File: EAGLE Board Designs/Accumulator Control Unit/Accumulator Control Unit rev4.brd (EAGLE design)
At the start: 186.7 x 135.7 mm, 241 parts, among them J1 CONNECTOR-2_MF_T_V_, J100 CONNECTOR-8_S_S, J2 CONNECTOR-8_MF_T_V_, J3 CONNECTOR-14_MF_T_V_, J4 JUMPER__1X02, J5 CONNECTOR-12_MF_T_V_, J6 CONNECTOR-CAN_μF_S_RA_, Q1 TRANSISTOR_N_MOS__PMV15ENEA, Q100 TRANSISTOR_N_MOS__PMV15ENEA, Q101 TRANSISTOR_N_MOS__PMV15ENEA, Q2 TRANSISTOR_N_MOS__PMV15ENEA, T1 TRANSFORMER_HM2112ZNLT_AIRGAP, U1 RELAY_SOLIDSTATE_NO, U10 MAX7404, U100 ADG1423, U101 LM555, U11 OPAMP_1_CHANNEL_OPA991, U12 LOGICGATE_AND_DCK3, U13 OPAMP_1_CHANNEL_OPA991, U14 LOGICGATE_AND_DCK3, U15 OPAMP_1_CHANNEL_OPA991, U16 LOGICGATE_AND_DCK3, U17 OPAMP_1_CHANNEL_OPA991, U18 OPAMP_1_CHANNEL_OPA991, U19 MAX7404, U2 RELAY_SOLIDSTATE_NO, U20 OPAMP_1_CHANNEL_OPA991, U21 OPAMP_1_CHANNEL_OPA991, U22 OPAMP_1_CHANNEL_OPA991, U23 OPAMP_1_CHANNEL_OPA991, U24 OPAMP_1_CHANNEL_OPA991, U25 MAX7404, U26 VOLTAGE_REGULATOR_SOT223_3.3V, U27 TCAN1051HQV-Q1, U3 OPAMP_1_CHANNEL_OPA991, U4 MAX7404, U5 LTC6820, U6 LOGICGATE_BUFFER, U7 ADM8316WBX30, U8 RELAY_SOLIDSTATE_NO, U9 OPAMP_1_CHANNEL_OPA991

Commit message: uncursed library
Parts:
- added A3: VOLTAGE_REGULATOR_MODULE_OKI-78SR_12V, HyTechDevices:OKI-78SR
- added TP1_24V: TEST_POINT, HyTechDevices:5015
- J3: device HyTechDevices - Copy:MOLEX_MICROFIT_PTH_VERTICAL_14_DUAL -> HyTechDevices:MOLEX_MICROFIT_PTH_VERTICAL_14_DUAL
- TP_12V, TP_3.3V, TP_5V, TP_GND: device HyTechDevices - Copy:MICRO_MINIATURE -> HyTechDevices:5015
- U1, U2, U8: value RELAY_SOLIDSTATE_NO -> RELAY_SOLIDSTATE_NO_DIP-4
- moved J3 80.7 mm to (-10.9, -32.5), turned to 0 degrees
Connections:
- net 12VIN renamed 24VIN
- new net +24V: A1.1, C24.1, J100.5, J2.1, J3.7, J6.1, TP1_24V.1, XF1.3, XF1.4
- new net IN: A3.1
- new net N$32: J3.12
- net +12V: no longer A1.1, C24.1, J100.5, J2.1, J3.7, J6.1, XF1.3, XF1.4
- net GND: now also A3.2
- net SHDN: no longer J3.12
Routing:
- net +12V: track 614.1 -> 541.0 mm
- net AIR2-: track 61.2 -> 45.6 mm
- net ACCUMULATOR_GND: track 151.2 -> 139.0 mm
- net CURRENT: track 189.0 -> 179.1 mm
- net CURRENT_REF: track 138.3 -> 128.6 mm
- net SHDN: track 97.3 -> 94.7 mm
- net CANH: track 230.1 -> 228.2 mm
- net +5V: track 565.8 -> 564.8 mm

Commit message: new voltage dividers
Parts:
- added C40, C7: CAPACITOR_0805_50V_10UF, HyTechDevices:0805-CAP
- A1: device HyTechDevices - Copy:OKI-78SR -> HyTechDevices:OKI-78SR
- C24: value CAPACITOR_0603_25V_10UF -> CAPACITOR_0805_50V_10UF; device HyTechDevices:0603-CAP -> HyTechDevices:0805-CAP
- R41, R48: value RESISTOR_0603_10.2K -> RESISTOR_0603_14K
- R49, R63: value RESISTOR_0603_4.12K -> RESISTOR_0603_1K
- R51: value RESISTOR_0603_11.5K -> RESISTOR_0603_5.9K
- R66, R67, R74, R75: value RESISTOR_0603_11.5K -> RESISTOR_0603_13K
- U26: value VOLTAGE_REGULATOR_SOT223_3.3V -> VOLTAGE_REGULATOR_SOT-223_3.3V; device HyTechDevices - Copy:SOT223 -> HyTechDevices:SOT-223
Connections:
- net 2.5_DIV renamed 3.305V_DIV
- net 3.56V_DIV_A renamed 4.66V_DIV_A
- net 3.56V_DIV_B renamed 4.66V_DIV_B
- removed net IN: A3.1
- removed net N$32: J3.12
- net +12V: now also A3.3, C40.1
- net +24V: now also A3.1, C7.1
- net GND: now also C40.2, C7.2
- net SHDN: now also J3.12

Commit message: more changes
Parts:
- removed D8: TVS_15V, HyTechDevices:SOT-23
- added 24V: LED_0603_ORANGE, HyTechDevices:0603-LED
- added R83: RESISTOR_0603_3.3K, HyTechDevices:0603-RES
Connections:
- new net N$32: 24V.1, R83.2
- net +24V: now also 24V.2
- net 24VIN: no longer D8.3
- net GND: now also R83.1; no longer D8.1
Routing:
- net 24VIN: track 98.8 -> 80.1 mm
- net +3V3: track 83.4 -> 75.1 mm, vias 24 -> 23
- net GND: track 225.6 -> 223.9 mm, vias 141 -> 140

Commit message: changed resistor dividers
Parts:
- added D1: TVS_30VDO-214AA, HyTechDevices:DO-214AA
- R12, R6: value RESISTOR_0603_10K -> RESISTOR_0603_20K
- R3, R9: value RESISTOR_0603_1K -> RESISTOR_0603_2K
- R38: value RESISTOR_0603_11.5K -> RESISTOR_0603_8.66K
- R39: value RESISTOR_0603_84.5K -> RESISTOR_0603_73.2K
- R40: value RESISTOR_0603_DNP -> RESISTOR_0603_1M
- R7: value RESISTOR_0603_2K -> RESISTOR_0603_5.1K
- R8: value RESISTOR_0603_2K -> RESISTOR_0603_5.1K; device HyTechDevices - Copy:0603-RES -> HyTechDevices:0603-RES
- moved R8 203.5 mm to (-22.1, -63.8), turned to 0 degrees
- moved R7 192.2 mm to (-22.1, -60.7), turned to 0 degrees
- moved R40 116.8 mm to (-22.1, -72.9), turned to 0 degrees
- moved R39 111.6 mm to (-22.1, -69.8), turned to 0 degrees
- moved R38 110.5 mm to (-22.1, -66.8), turned to 0 degrees
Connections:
- net +12V: no longer R7.2, U1.4, U2.4
- net +24V: now also R7.2, U1.4, U2.4
- net 24VIN: now also D1.2
- net GND: now also D1.1
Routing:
- net +12V: track 541.0 -> 523.0 mm
- net +24V: track 0.00 -> 12.7 mm
- net N$16: track 8.37 -> 3.92 mm
- net 0.5989V_DIV: track 5.25 -> 1.89 mm
- net N$8: track 4.07 -> 0.82 mm
- net GND: track 223.9 -> 221.3 mm, vias 140 -> 138
- net OKHS: track 34.5 -> 32.9 mm
- net +5V: track 564.8 -> 563.8 mm

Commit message: changed more resistor dividers
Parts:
- removed D10, D9: TVS_15V, HyTechDevices:SOT-23
- removed R107: RESISTOR_0603_12K, HyTechDevices - Copy:0603-RES
- removed R108: RESISTOR_0603_, HyTechDevices:0603-RES
- added D5, D6: TVS_30VDO-214AA, HyTechDevices:DO-214AA
- added R84: RESISTOR_0603_5.1K, HyTechDevices:0603-RES
- added R85: RESISTOR_0603_33K, HyTechDevices:0603-RES
- D3, D7: value TVS_15V -> TVS_30VDO-214AA; device HyTechDevices:SOT-23 -> HyTechDevices:DO-214AA
- R21: value RESISTOR_0603_15K -> RESISTOR_0603_5.1K
- R4: value RESISTOR_0603_ -> RESISTOR_0603_5.1K
- R5: value RESISTOR_0603_12K -> RESISTOR_0603_33K; device HyTechDevices - Copy:0603-RES -> HyTechDevices:0603-RES
- R79: value RESISTOR_0603_ -> RESISTOR_0603_33K
- R80: value RESISTOR_0603_12K -> RESISTOR_0603_5.1K; device HyTechDevices - Copy:0603-RES -> HyTechDevices:0603-RES
- moved D3 246.1 mm to (-21.6, -104.4), turned to 0 degrees
- moved R21 236.0 mm to (-22.9, -99.8), turned to 0 degrees
- moved R80 216.4 mm to (-23.9, -117.6), turned to 0 degrees
- moved R79 215.1 mm to (-23.4, -114.6)
- moved R5 204.6 mm to (-22.1, -79.0)
- moved R4 203.4 mm to (-22.1, -75.9), turned to 0 degrees
- moved D7 192.5 mm to (-21.6, -110.2)
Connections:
- removed net 12V_SCALED_3.3V: A2.D19, R107.1, R108.2
- new net 24V_SCALED_3.3V: A2.D19, R84.1, R85.2
- net +12V: no longer D7.3, R108.1
- net +24V: now also D6.2, R85.1
- net BSPD_CURRENT: now also D7.2; no longer D9.3
- net GND: now also D5.1, D6.1, R4.2, R84.2; no longer D10.1, D9.1, R107.2, R5.2
- net IMD_OK: now also D5.2, R5.1; no longer D10.3, R4.1
- net IMD_OK_TEENSY: now also R4.1, R5.2; no longer R4.2, R5.1
- net MHS: now also D3.2; no longer D3.3
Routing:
- net 12V_SCALED_3.3V: track 23.4 -> 0.00 mm
- net 24V_SCALED_3.3V: track 0.00 -> 21.6 mm
- net +12V: track 523.0 -> 510.0 mm
- net GND: track 221.3 -> 208.5 mm, vias 138 -> 130
- net BSPD_CURRENT_TEENSY: track 28.4 -> 22.0 mm
- net IMD_OK: track 176.9 -> 173.9 mm
- net IMD_OK_TEENSY: track 113.5 -> 110.7 mm
- net MHS_TEENSY: track 51.1 -> 49.4 mm
- net MHS: track 20.3 -> 19.3 mm

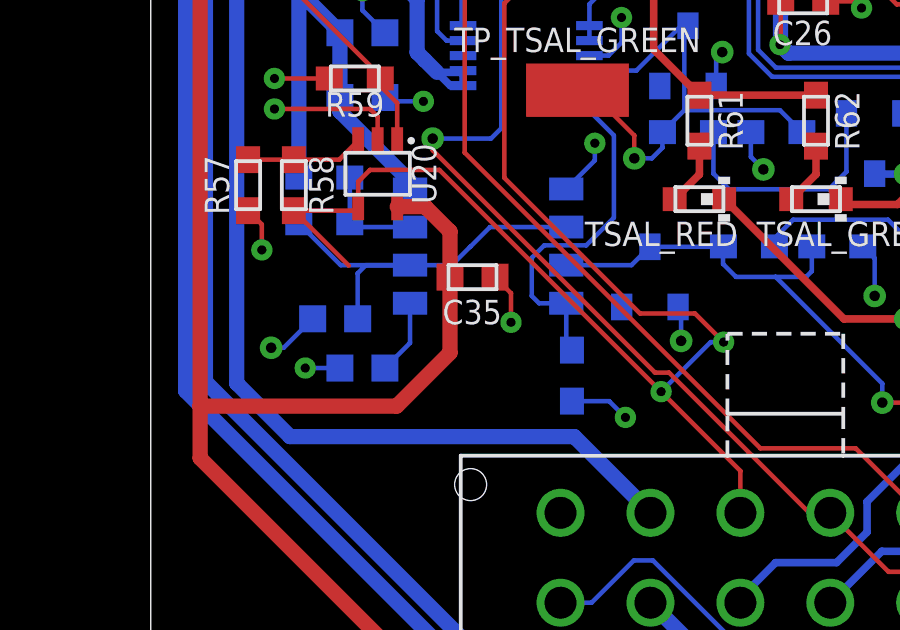
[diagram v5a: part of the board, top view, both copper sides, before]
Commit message: bspd current signal changes
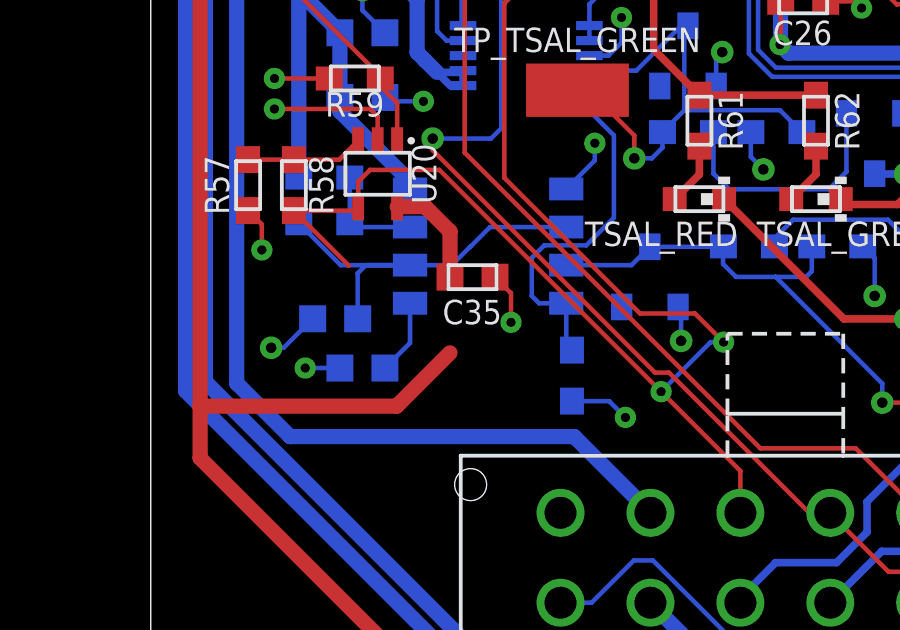
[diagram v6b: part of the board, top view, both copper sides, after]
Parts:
- C35: value CAPACITOR_0603_25V_0.1UF -> CAPACITOR_0603_50V_0.1UF
- R57: value RESISTOR_0603_1K -> RESISTOR_0603_10K; device HyTechDevices - Copy:0603-RES -> HyTechDevices:0603-RES
- R58: value RESISTOR_0603_1.4K -> RESISTOR_0603_30K; device HyTechDevices - Copy:0603-RES -> HyTechDevices:0603-RES
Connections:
- net +12V: no longer C35.1, U20.5
- net +24V: now also C35.1, U20.5
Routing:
- net +12V: track 510.0 -> 503.9 mm
- net +24V: track 12.7 -> 16.3 mm

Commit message: changed bspd resistor divider
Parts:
- R57: value RESISTOR_0603_10K -> RESISTOR_0603_2.74K
- R58: value RESISTOR_0603_30K -> RESISTOR_0603_10.5K
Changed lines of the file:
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@@
 <attribute name="VOLTAGE_MAX" value="50V" x="126.5936" y="-10.721275" size="1.778" layer="27" display="off"/>
 </element>
-<element name="R57" library="HyTechDevices" package="0603-RES" value="RESISTOR_0603_10K" x="3.24529375" y="21.47251875" smashed="yes" rot="R90">
-<attribute name="DKPN" value="311-10.0KHRCT-ND" x="90.87529375" y="109.10251875" size="1.778" layer="27" rot="R90" display="off"/>
-<attribute name="MANUFACTURER" value="Yageo" x="90.87529375" y="109.10251875" size="1.778" layer="27" rot="R90" display="off"/>
-<attribute name="MOPN" value="603-RC0603FR-0710KL" x="90.87529375" y="109.10251875" size="1.778" layer="27" rot="R90" display="off"/>
-<attribute name="MPN" value="RC0603FR-0710KL" x="90.87529375" y="109.10251875" size="1.778" layer="27" rot="R90" display="off"/>
+<element name="R57" library="HyTechDevices" package="0603-RES" value="RESISTOR_0603_2.74K" x="3.24529375" y="21.47251875" smashed="yes" rot="R90">
+<attribute name="DKPN" value="P20020CT-ND" x="90.87529375" y="109.10251875" size="1.778" layer="27" rot="R90" display="off"/>
+<attribute name="MANUFACTURER" value="Panasonic Electronic Components" x="90.87529375" y="109.10251875" size="1.778" layer="27" rot="R90" display="off"/>
+<attribute name="MOPN" value="667-ERJ-PB3B2741V" x="90.87529375" y="109.10251875" size="1.778" layer="27" rot="R90" display="off"/>
+<attribute name="MPN" value="ERJ-PB3B2741V" x="90.87529375" y="109.10251875" size="1.778" layer="27" rot="R90" display="off"/>
 <attribute name="NAME" x="2.61029375" y="21.47251875" size="0.8128" layer="25" font="vector" rot="R90" align="bottom-center"/>
-<attribute name="POWER" value="0.1W" x="90.87529375" y="109.10251875" size="1.778" layer="27" rot="R90" display="off"/>
-<attribute name="RESISTANCE" value="10k" x="90.87529375" y="109.10251875" size="1.778" layer="27" rot="R90" display="off"/>
-<attribute name="TOLERANCE" value="1%" x="90.87529375" y="109.10251875" size="1.778" layer="27" rot="R90" display="off"/>
-<attribute name="VOLTAGE_CONTINUOUS" value="31.62V" x="90.87529375" y="109.10251875" size="1.778" layer="27" rot="R90" display="off"/>
-<attribute name="VOLTAGE_MAX" value="75V" x="90.87529375" y="109.10251875" size="1.778" layer="27" rot="R90" display="off"/>
+<attribute name="POWER" value="0.2W" x="90.87529375" y="109.10251875" size="1.778" layer="27" rot="R90" display="off"/>
+<attribute name="RESISTANCE" value="2.74k" x="90.87529375" y="109.10251875" size="1.778" layer="27" rot="R90" display="off"/>
+<attribute name="TOLERANCE" value="0.1%" x="90.87529375" y="109.10251875" size="1.778" layer="27" rot="R90" display="off"/>
+<attribute name="VOLTAGE_CONTINUOUS" value="23.41V" x="90.87529375" y="109.10251875" size="1.778" layer="27" rot="R90" display="off"/>
+<attribute name="VOLTAGE_MAX" value="150V" x="90.87529375" y="109.10251875" size="1.778" layer="27" rot="R90" display="off"/>
 </element>
-<element name="R58" library="HyTechDevices" package="0603-RES" value="RESISTOR_0603_30K" x="4.76929375" y="21.47251875" smashed="yes" rot="R270">
-<attribute name="DKPN" value="P30KBDCT-ND" x="-86.67070625" y="6.23251875" size="1.778" layer="27" rot="R270" display="off"/>
+<element name="R58" library="HyTechDevices" package="0603-RES" value="RESISTOR_0603_10.5K" x="4.76929375" y="21.47251875" smashed="yes" rot="R270">
+<attribute name="DKPN" value="P10.5KDBCT-ND" x="-86.67070625" y="6.23251875" size="1.778" layer="27" rot="R270" display="off"/>
 <attribute name="MANUFACTURER" value="Panasonic Electronic Components" x="-86.67070625" y="6.23251875" size="1.778" layer="27" rot="R270" display="off"/>
-<attribute name="MOPN" value="667-ERA-3ARB303V" x="-86.67070625" y="6.23251875" size="1.778" layer="27" rot="R270" display="off"/>
-<attribute name="MPN" value="ERA-3ARB303V" x="-86.67070625" y="6.23251875" size="1.778" layer="27" rot="R270" display="off"/>
+<attribute name="MOPN" value="677-ERA-3AEB1052V" x="-86.67070625" y="6.23251875" size="1.778" layer="27" rot="R270" display="off"/>
+<attribute name="MPN" value="ERA-3AEB1052V" x="-86.67070625" y="6.23251875" size="1.778" layer="27" rot="R270" display="off"/>
 <attribute name="NAME" x="5.27729375" y="21.47251875" size="0.8128" layer="25" font="vector" rot="R270" align="bottom-center"/>
 <attribute name="POWER" value="0.1W" x="-86.67070625" y="6.23251875" size="1.778" layer="27" rot="R270" display="off"/>
-<attribute name="RESISTANCE" value="30k" x="-86.67070625" y="6.23251875" size="1.778" layer="27" rot="R270" display="off"/>
+<attribute name="RESISTANCE" value="10.5k" x="-86.67070625" y="6.23251875" size="1.778" layer="27" rot="R270" display="off"/>
 <attribute name="TOLERANCE" value="0.1%" x="-86.67070625" y="6.23251875" size="1.778" layer="27" rot="R270" display="off"/>
-<attribute name="VOLTAGE_CONTINUOUS" value="54.77V" x="-86.67070625" y="6.23251875" size="1.778" layer="27" rot="R270" display="off"/>
+<attribute name="VOLTAGE_CONTINUOUS" value="32.40V" x="-86.67070625" y="6.23251875" size="1.778" layer="27" rot="R270" display="off"/>
 <attribute name="VOLTAGE_MAX" value="75V" x="-86.67070625" y="6.23251875" size="1.778" layer="27" rot="R270" display="off"/>
 </element>

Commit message: changed descriptions
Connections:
- net 0.5989V_DIV renamed 0.526V_DIV
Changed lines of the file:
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@@
 <wire x1="43.11731875" y1="36.80288125" x2="42.2012" y2="37.719" width="0.1524" layer="1"/>
 </signal>
-<signal name="0.5989V_DIV">
+<signal name="0.526V_DIV">
 <contactref element="U21" pad="3"/>
 <wire x1="23.25470625" y1="30.40928125" x2="23.25470625" y2="32.30328125" width="0.1524" layer="1"/>
